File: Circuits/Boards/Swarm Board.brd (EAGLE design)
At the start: 63.5 x 63.5 mm, 89 parts, among them CON1 ISP(2X3), T1 NPN2N2222, T10 TEFT4300, T13 NPN2N2222, T14 NPN2N2222, T15 NPN2N2222, T16 NPN2N2222, T17 NPN2N2222, T18 NPN2N2222, T2 NPN2N2222, T3 NPN2N2222, T4 TEFT4300, T5 TEFT4300, T6 TEFT4300, T7 TEFT4300, T8 TEFT4300, T9 TEFT4300, U1 ATMEGA324P, U2 MCP73832SOT-23, U3 TB6552FN/FNG

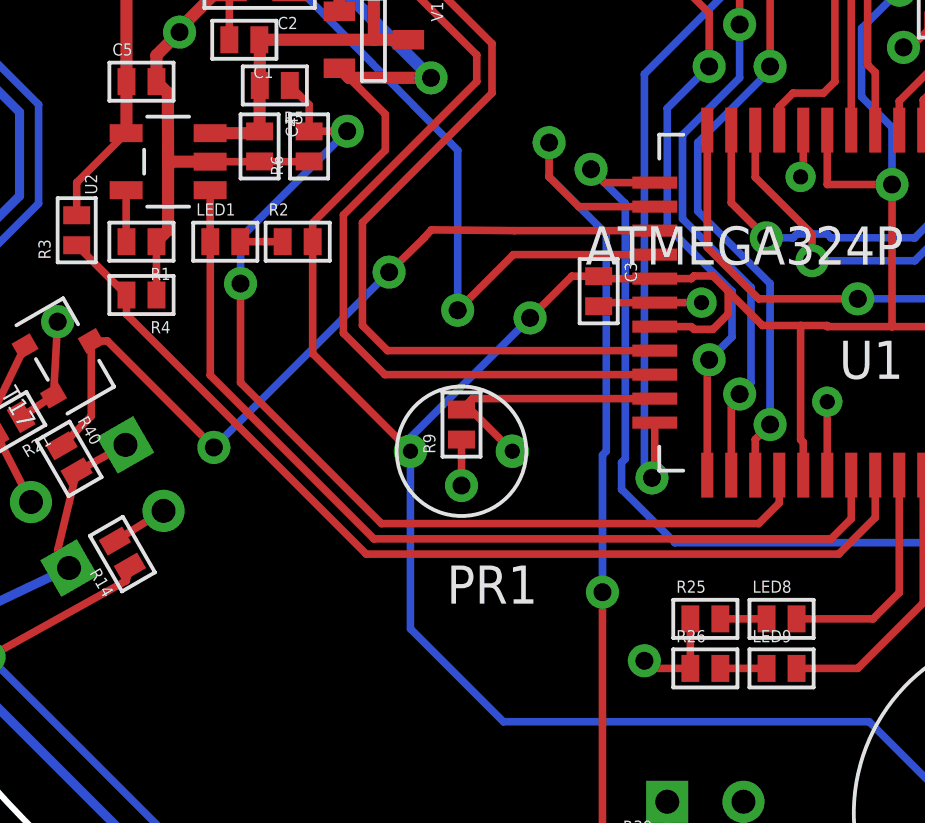
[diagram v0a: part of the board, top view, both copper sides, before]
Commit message: 
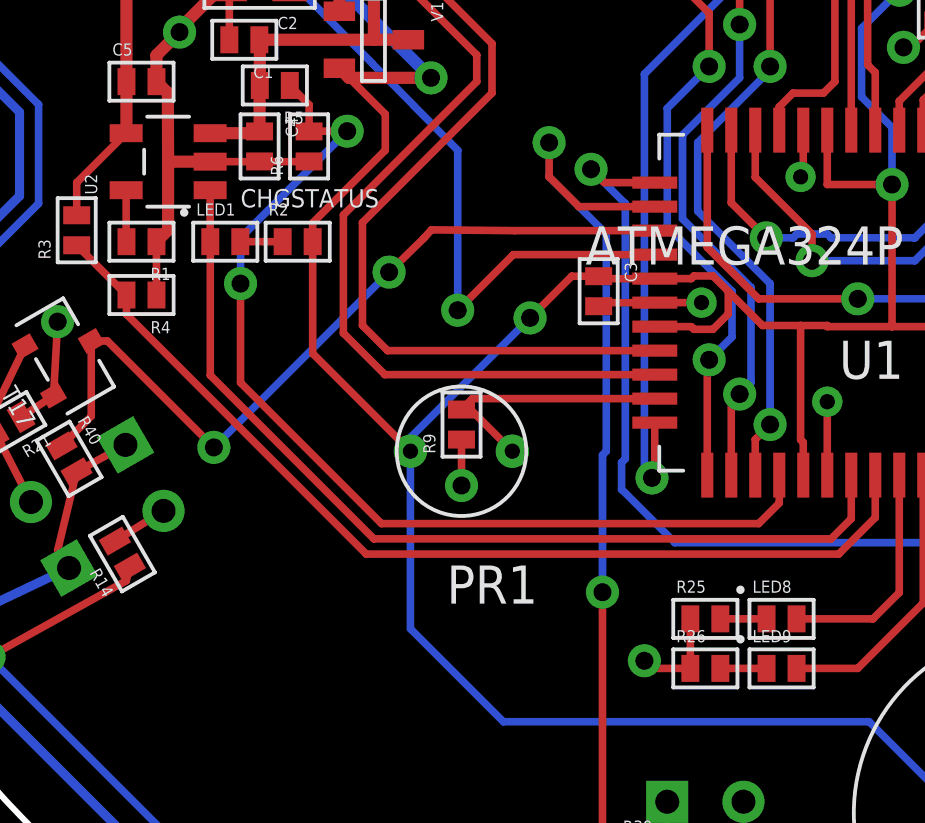
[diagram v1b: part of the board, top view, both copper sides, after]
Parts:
- LED1, LED8, LED9: device Passive:0603 -> Passive:LED0603
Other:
- board text added: "CHGSTATUS"
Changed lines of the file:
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@@
 <text x="30.988" y="49.022" size="0.6096" layer="21">PWR</text>
 <text x="43.307" y="49.022" size="0.6096" layer="21">DATA</text>
+<text x="16.256" y="29.972" size="0.6096" layer="21">CHGSTATUS</text>
 </plain>
 <attributes>
@@
 <element name="LED13" library="Passive" package="5MM_LED_RA" value="IR" x="27.94" y="53.34" rot="MR0"/>
 <element name="C7" library="Passive" package="0805" value="10uf" x="22.987" y="59.309" rot="R180"/>
-<element name="LED1" library="Passive" package="0603" value="red" x="15.748" y="28.829"/>
+<element name="LED1" library="Passive" package="LED0603" value="red" x="15.748" y="28.829"/>
 <element name="T4" library="Passive" package="3MM_LED_RA" value="TEFT4300" x="35.56" y="57.15"/>
 <element name="T5" library="Passive" package="3MM_LED_RA" value="TEFT4300" x="53.68795" y="44.4202875" rot="R300"/>
@@
 <element name="C8" library="Passive" package="0603" value="1uf" x="39.497" y="36.703" rot="R270"/>
 <element name="C9" library="Passive" package="0603" value="1uf" x="46.863" y="40.005" rot="R270"/>
-<element name="LED8" library="Passive" package="0603" value="red" x="34.29" y="16.256"/>
+<element name="LED8" library="Passive" package="LED0603" value="red" x="34.29" y="16.256"/>
 <element name="R25" library="Passive" package="0603" value="750" x="31.75" y="16.256"/>
-<element name="LED9" library="Passive" package="0603" value="green" x="34.29" y="14.605"/>
+<element name="LED9" library="Passive" package="LED0603" value="green" x="34.29" y="14.605"/>
 <element name="R26" library="Passive" package="0603" value="750" x="31.75" y="14.605"/>
 <element name="R28" library="Passive" package="0603" value="1k" x="42.799" y="14.732"/>
